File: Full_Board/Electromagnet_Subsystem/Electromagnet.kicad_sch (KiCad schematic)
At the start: 3 parts, among them IC5 BD62130AEFJ-E2

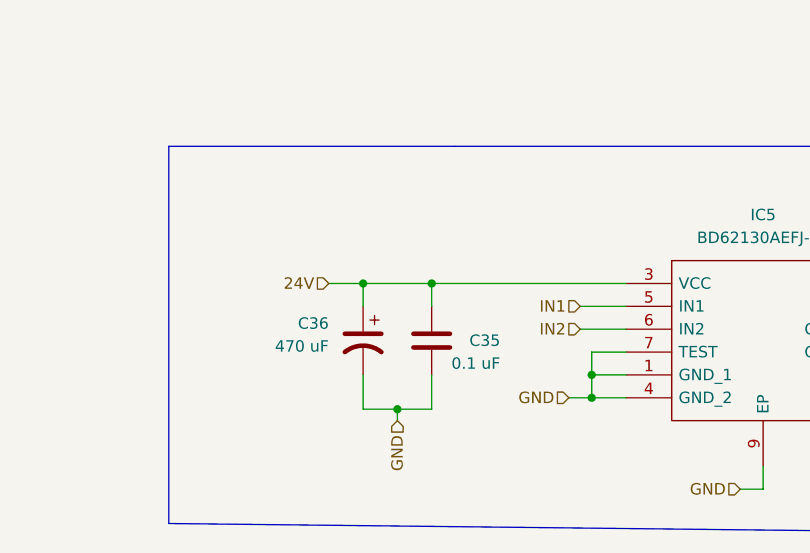
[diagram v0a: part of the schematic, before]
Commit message: Added traces for emag and increased the width of some power lines
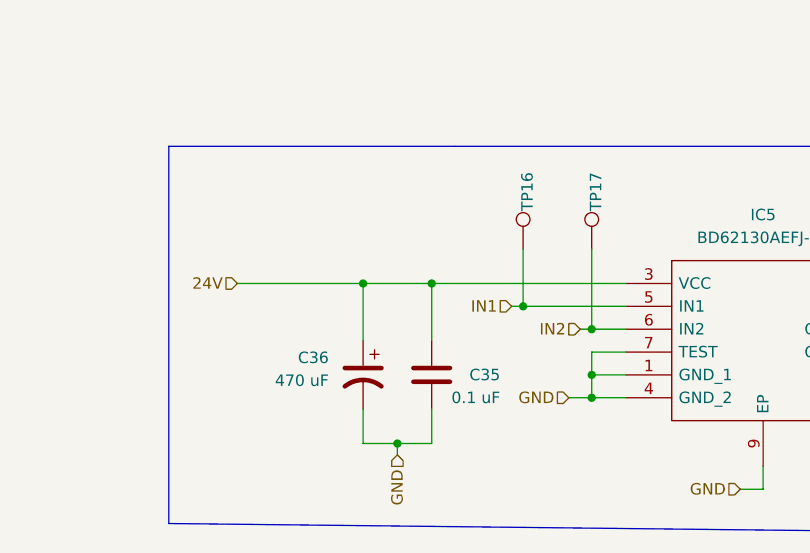
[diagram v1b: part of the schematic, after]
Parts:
- added TP16, TP17: ~, TestPoint:TestPoint_Keystone_5010-5014_Multipurpose, symbol Connector:TestPoint
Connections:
- net IN1: now also TP16.1
- net IN2: now also TP17.1
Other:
- moved on the sheet: C35, C36

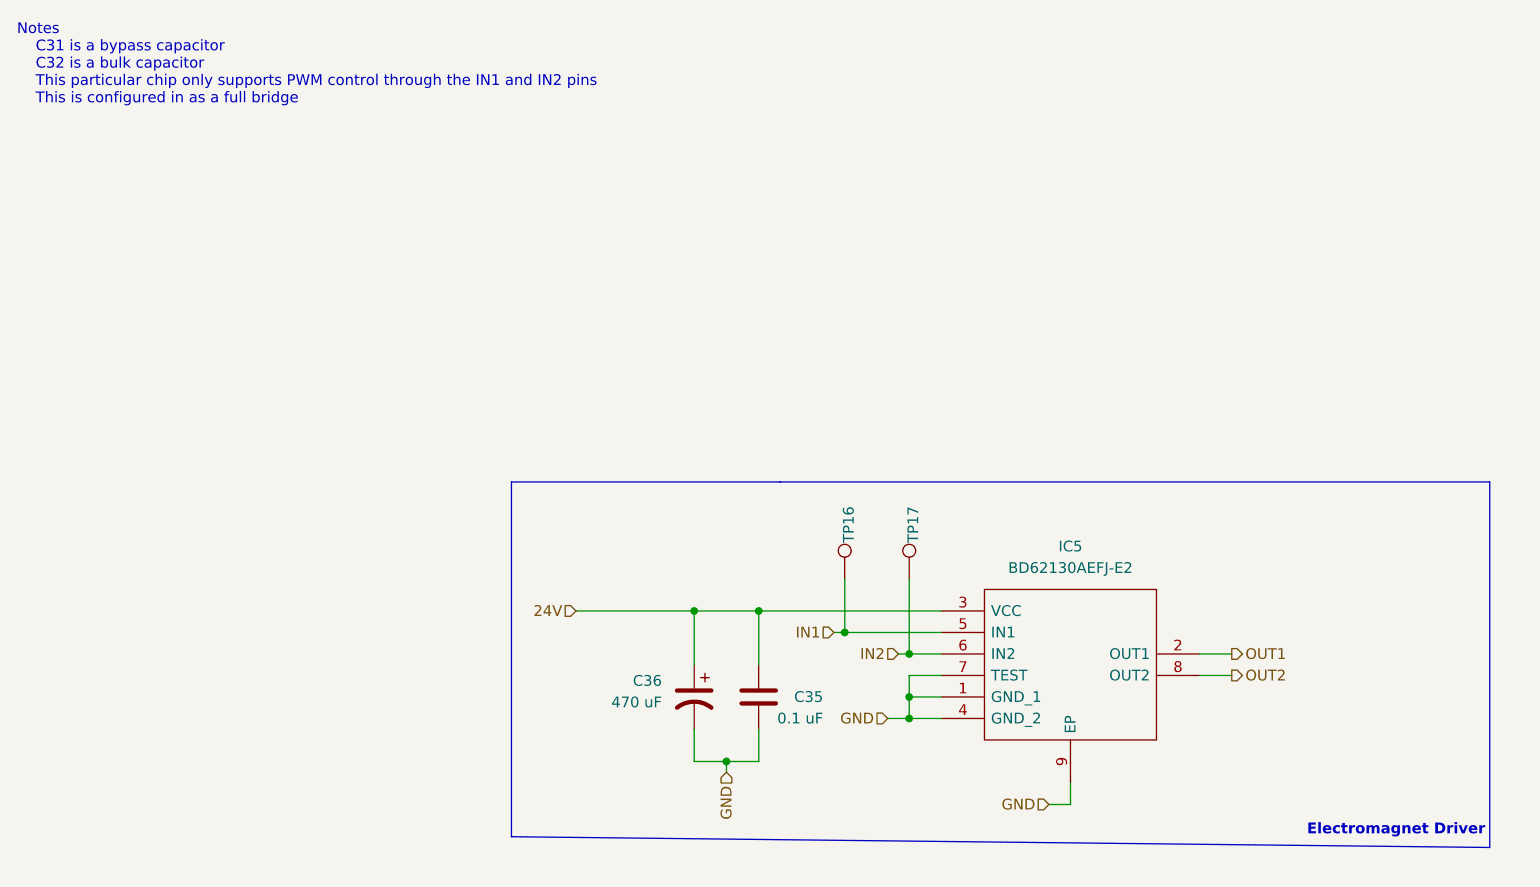
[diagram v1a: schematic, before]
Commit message: Cleanup all schematics and project libs
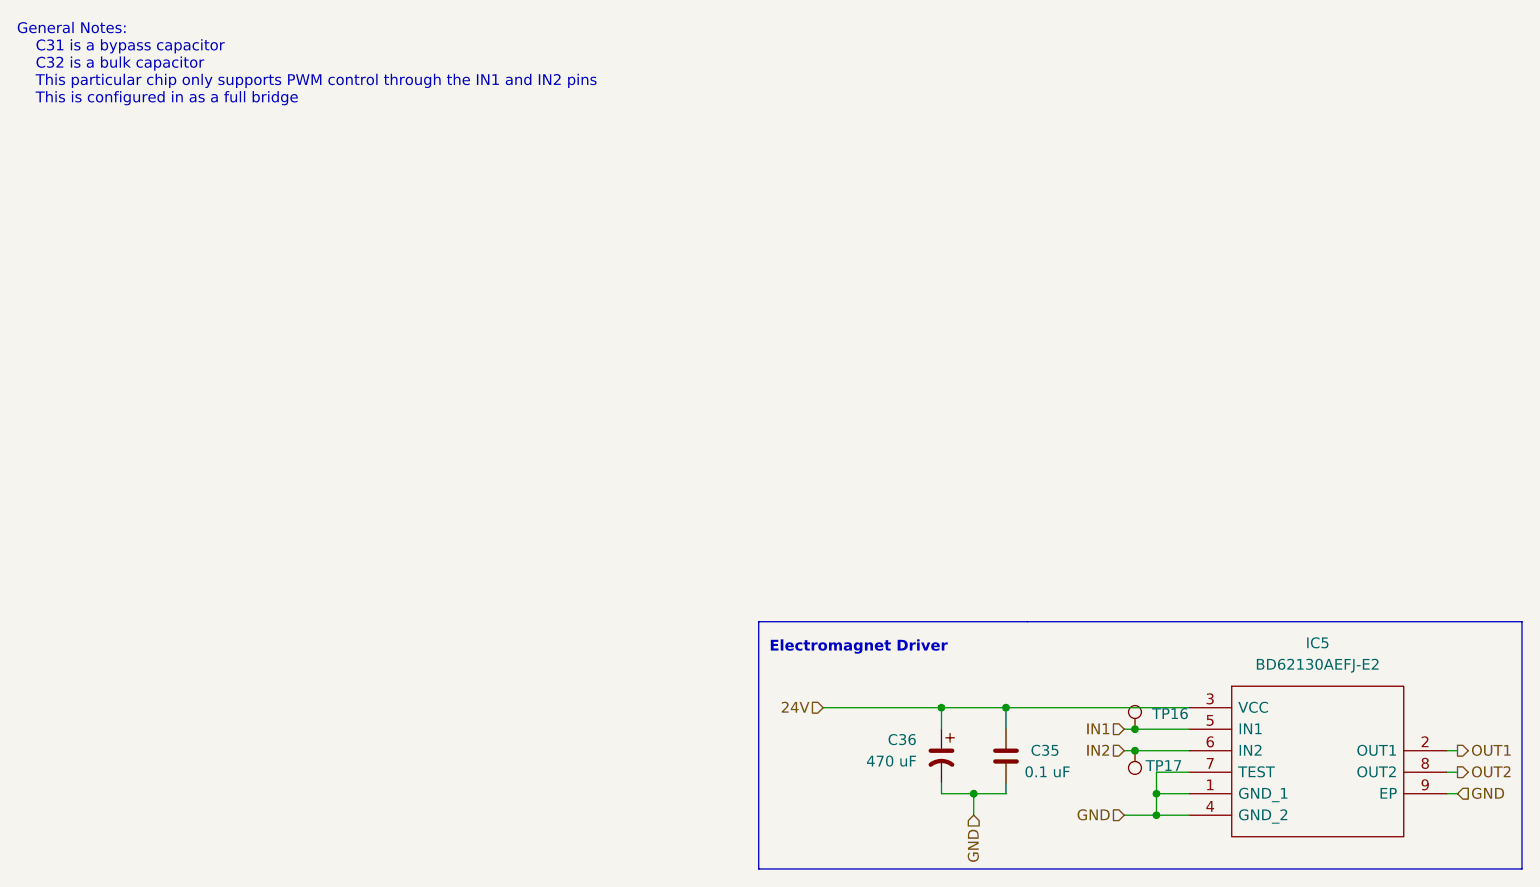
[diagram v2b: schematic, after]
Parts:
- C35: symbol Device:C -> CL10B104KB8NNC:CL10B104KB8NNNC; Digikey Link https://www.digikey.com/en/products/detail/samsung-electro-mechanics/CL10B104KB8NNNC/3886658 -> https://www.digikey.com/en/products/detail/samsung-electro-mechanics/CL10B104KB8NNNC/3886658?s=N4IgTCBcDaIMIBkCMAGAQqgLAaTQDgDki4QBdAXyA; Digikey Part Number 1276-1000-6-ND -> 1276-1000-1-ND; Manufacturer's Part Number (none) -> CL10B104KB8NNNC; Manufacturers Part Number CL10B104KB8NNNC -> (none); Mouser Link (none) -> https://www.mouser.com/ProductDetail/Samsung-Electro-Mechan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; Mouser Part Number (none) -> 187-CL10B104KB8NNNC
- C36: footprint EEE-FP1E471AP:EEE-FP1E471AP -> CAP_EEFK_G_PAN; symbol Device:C_Polarized_US -> EEE-FP1E471AP:470uF; Digikey Link https://www.digikey.com/en/products/detail/panasonic-electronic-components/EEE-FP1E471AP/1245939 -> https://www.digikey.com/en/products/detail/panasonic-electronic-components/EEE-FP1E471AP/1245939?s=N4IgTCBcDaIKIILQDEAKBGOAWA7OggqiALoC%2BQA; Digikey Part Number PCE4440DKR-ND -> PCE4440CT-ND; Manufacturer's Part Number (none) -> EEE-FP1E471AP; Manufacturers Part Number EEE-FP1E471AP -> (none); Mouser Link (none) -> https://www.mouser.com/ProductDetail/Panasonic/EEE-FP1E471A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; Mouser Part Number (none) -> 667-EEE-FP1E471AP
- IC5: Digikey Link https://www.digikey.com/en/products/detail/rohm-semiconductor/BD62130AEFJ-E2/10233247 -> https://www.digikey.com/en/products/detail/rohm-semiconductor/BD62130AEFJ-E2/10233247?s=N4IgTCBcDaIEIBEBsYCMBmADAQQKIDEApAWlwgF0BfIA; Digikey Part Number BD62130AEFJ-E2DKR-ND -> BD62130AEFJ-E2CT-ND; Height 1 -> (none); Manufacturer's Part Number (none) -> BD62130AEFJ-E2; Manufacturer_Name ROHM Semiconductor -> (none); Manufacturer_Part_Number BD62130AEFJ-E2 -> (none); Mouser Price/Stock https://www.mouser.co.uk/ProductDetail/ROHM-Semiconductor/B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 -> (none)
- TP16, TP17: value ~ -> TestPoint; symbol Connector:TestPoint -> 5010:5010; Digikey Link (none) -> https://www.digikey.com/en/products/detail/keystone-electro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; Digikey link https://www.digikey.com/en/products/detail/keystone-electro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 -> (none); Mouser Link (none) -> https://www.mouser.com/ProductDetail/Keystone-Electronics/5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; Mouser link https://www.mouser.com/ProductDetail/Keystone-Electronics/5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 -> (none)
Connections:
- net IN1: now also TP16.; no longer TP16.1
- net IN2: now also TP17.; no longer TP17.1
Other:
- note added: "General Notes: C31 is a bypass capacitor C32 is a bulk capacitor This particular chip only supports PWM control through the IN1 and IN2 pins This is configured in as a full bridge"
- note removed: "Notes C31 is a bypass capacitor C32 is a bulk capacitor This particular chip only supports PWM control through the IN1 and IN2 pins This is configured in as a full bridge"
- moved on the sheet: C35, C36, IC5, TP16, TP17
